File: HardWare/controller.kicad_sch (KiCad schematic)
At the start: 60 parts, among them J2 hall, J3 Conn_01x03, Q1 Q_NMOS_SGD, Q2 Q_NMOS_SGD, Q3 Q_NMOS_SGD, Q4 Q_NMOS_SGD, Q5 Q_NMOS_SGD, Q6 Q_NMOS_SGD, U2 DRV8301DCAR

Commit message: Add PCB
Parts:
- J2: footprint Connector_Molex:Molex_CLIK-Mate_502382-0570_1x05-1MP_P1.25mm_Vertical -> Connector_Molex:Molex_CLIK-Mate_502386-0570_1x05-1MP_P1.25mm_Horizontal
- J3: footprint Connector:Banana_Jack_3Pin -> USER:MR30-M
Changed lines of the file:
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@@
       (effects (font (size 1.27 1.27)) (justify left))
     )
-    (property "Footprint" "Connector_Molex:Molex_CLIK-Mate_502382-0570_1x05-1MP_P1.25mm_Vertical" (id 2) (at 269.24 36.83 0)
+    (property "Footprint" "Connector_Molex:Molex_CLIK-Mate_502386-0570_1x05-1MP_P1.25mm_Horizontal" (id 2) (at 269.24 36.83 0)
       (effects (font (size 1.27 1.27)) hide)
     )
@@
       (effects (font (size 1.27 1.27)) (justify left))
     )
-    (property "Footprint" "Connector:Banana_Jack_3Pin" (id 2) (at 274.32 121.92 0)
-      (effects (font (size 1.27 1.27)) hide)
-    )
+    (property "Footprint" "USER:MR30-M" (id 2) (at 274.32 121.92 0)
+      (effects (font (size 1.27 1.27)) hide)
+    )

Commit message: Add Rules
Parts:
- TP1: footprint TestPoint:TestPoint_THTPad_D2.0mm_Drill1.0mm -> TestPoint:TestPoint_Pad_1.0x1.0mm
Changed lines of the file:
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@@
       (effects (font (size 1.27 1.27)) (justify left))
     )
-    (property "Footprint" "TestPoint:TestPoint_THTPad_D2.0mm_Drill1.0mm" (id 2) (at 96.52 34.29 0)
+    (property "Footprint" "TestPoint:TestPoint_Pad_1.0x1.0mm" (id 2) (at 96.52 34.29 0)
       (effects (font (size 1.27 1.27)) hide)
     )

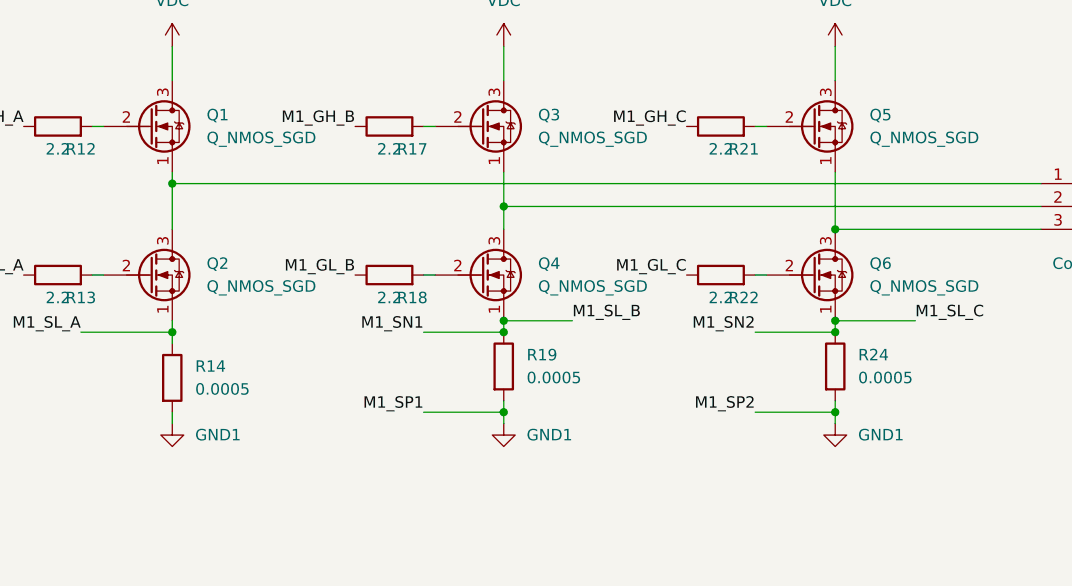
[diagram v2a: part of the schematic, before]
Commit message: 增加一些功率器件有关的pcb电路
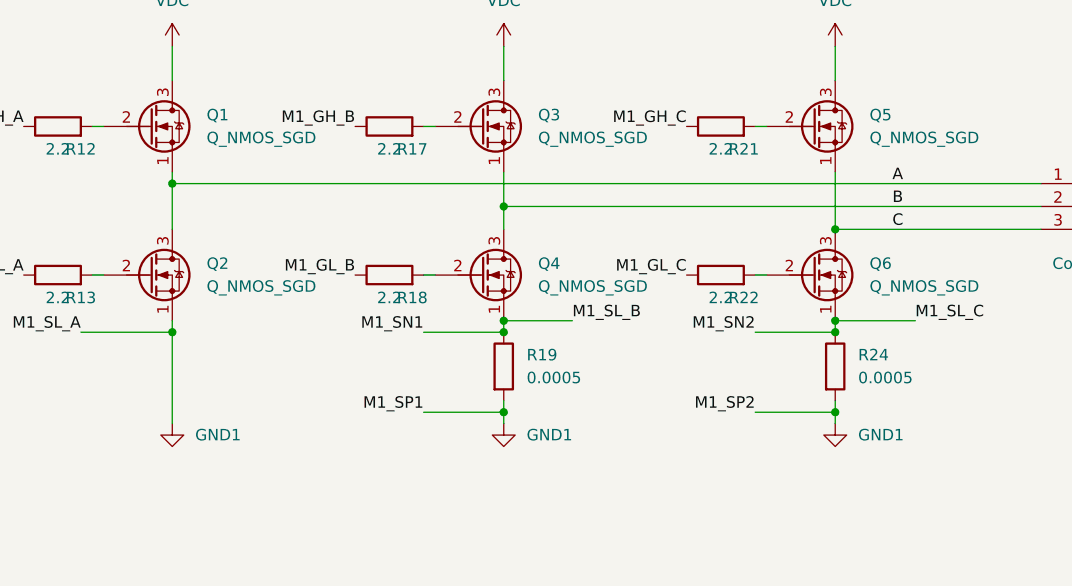
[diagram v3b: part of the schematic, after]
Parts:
- removed R14: 0.0005, Resistor_SMD:R_2512_6332Metric, symbol Device:R
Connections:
- net M1_SL_A is gone; now on net GND1: Q2.1 (S), U2.44 (SL_A)
- net A: now reaches J3.1 (Pin_1), Q1.1 (S), Q2.3 (D)
- net B: now reaches J3.2 (Pin_2), Q3.1 (S), Q4.3 (D)
- net C: now reaches J3.3 (Pin_3), Q5.1 (S), Q6.3 (D)
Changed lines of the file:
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@@
     (stroke (width 0) (type default) (color 0 0 0 0))
   )
-  (wire (pts (xy 172.72 144.78) (xy 172.72 146.05))
+  (wire (pts (xy 172.72 135.89) (xy 172.72 146.05))
     (stroke (width 0) (type default) (color 0 0 0 0))
   )
@@
     (stroke (width 0) (type default) (color 0 0 0 0))
   )
-  (wire (pts (xy 172.72 137.16) (xy 172.72 135.89))
-    (stroke (width 0) (type default) (color 0 0 0 0))
-  )
   (wire (pts (xy 240.03 36.83) (xy 264.16 36.83))
     (stroke (width 0) (type default) (color 0 0 0 0))
@@
     (effects (font (size 1.27 1.27)) (justify right bottom))
   )
+  (label "C" (at 252.73 124.46 0)
+    (effects (font (size 1.27 1.27)) (justify left bottom))
+  )
   (label "M1_GH_B" (at 193.04 113.03 180)
     (effects (font (size 1.27 1.27)) (justify right bottom))
@@
   )
   (label "SW_BST" (at 92.71 85.09 0)
+    (effects (font (size 1.27 1.27)) (justify left bottom))
+  )
+  (label "A" (at 252.73 119.38 0)
+    (effects (font (size 1.27 1.27)) (justify left bottom))
+  )
+  (label "B" (at 252.73 121.92 0)
     (effects (font (size 1.27 1.27)) (justify left bottom))
   )
@@
       (effects (font (size 1.27 1.27)) hide)
     )
-    (pin "1")
-    (pin "2")
-  )
-  (symbol (lib_id "Device:R") (at 172.72 140.97 0) (unit 1)
-    (in_bom yes) (on_board yes) (fields_autoplaced)
-    (property "Reference" "R14" (id 0) (at 175.26 139.6999 0)
-      (effects (font (size 1.27 1.27)) (justify left))
-    )
-    (property "Value" "0.0005" (id 1) (at 175.26 142.2399 0)
-      (effects (font (size 1.27 1.27)) (justify left))
-    )
-    (property "Footprint" "Resistor_SMD:R_2512_6332Metric" (id 2) (at 170.942 140.97 90)
-      (effects (font (size 1.27 1.27)) hide)
-    )
-    (property "Datasheet" "~" (id 3) (at 172.72 140.97 0)
-      (effects (font (size 1.27 1.27)) hide)
-    )

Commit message: 修改一些BUG
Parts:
- J2: footprint Connector_Molex:Molex_CLIK-Mate_502386-0570_1x05-1MP_P1.25mm_Horizontal -> USER:M1010RS-05P
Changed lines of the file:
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@@
       (effects (font (size 1.27 1.27)) (justify left))
     )
-    (property "Footprint" "Connector_Molex:Molex_CLIK-Mate_502386-0570_1x05-1MP_P1.25mm_Horizontal" (id 2) (at 269.24 36.83 0)
+    (property "Footprint" "USER:M1010RS-05P" (id 2) (at 269.24 36.83 0)
       (effects (font (size 1.27 1.27)) hide)
     )

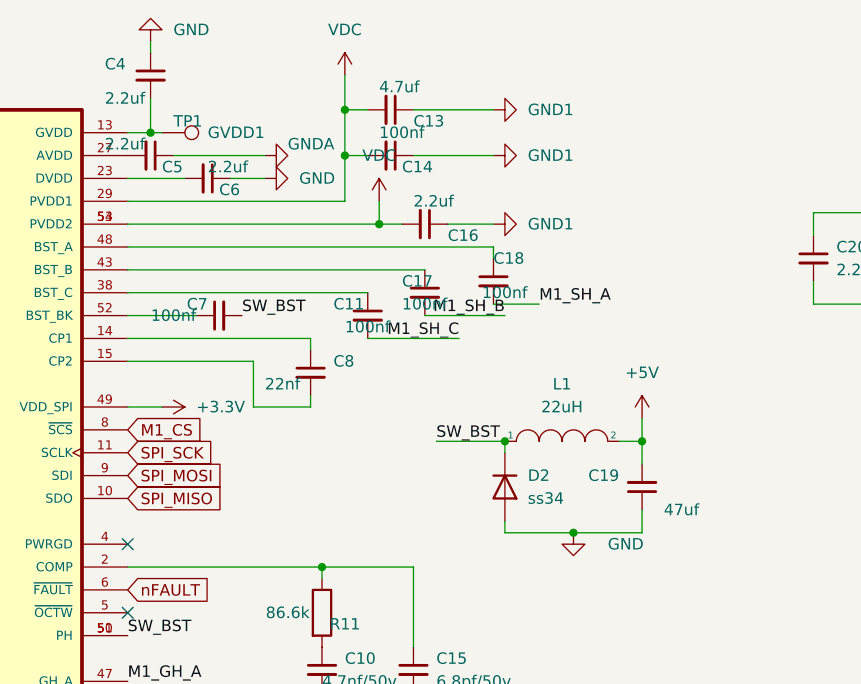
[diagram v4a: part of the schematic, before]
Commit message: 更新一些信号电源
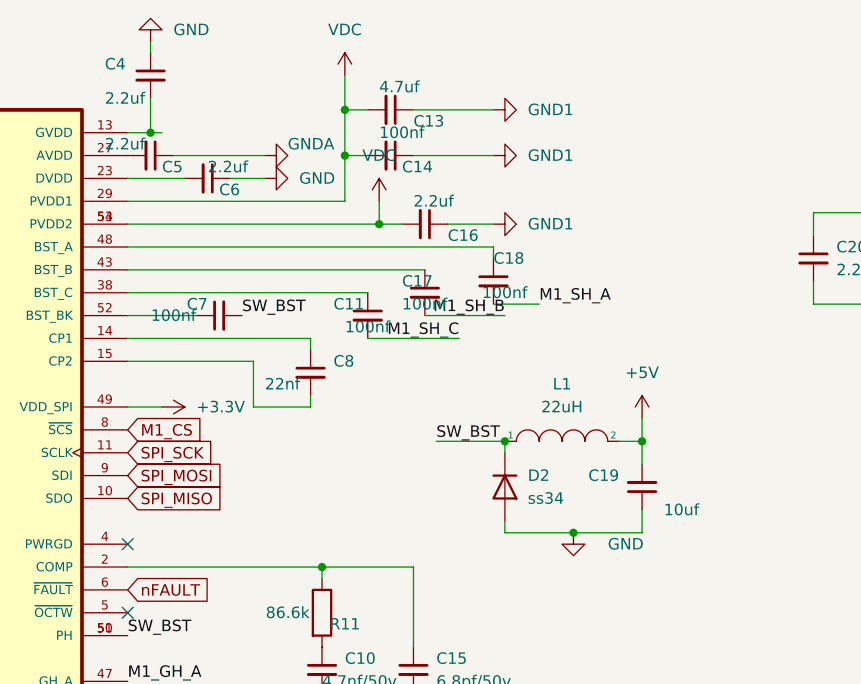
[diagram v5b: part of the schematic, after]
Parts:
- removed TP1: GVDD1, TestPoint:TestPoint_Pad_1.0x1.0mm, symbol Connector:TestPoint
- C19: value 47uf -> 10uf; footprint Capacitor_SMD:C_1812_4532Metric -> Capacitor_SMD:C_1210_3225Metric
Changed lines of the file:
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@@
       (effects (font (size 1.27 1.27)) (justify left))
     )
-    (property "Value" "47uf" (id 1) (at 156.21 71.12 0)
+    (property "Value" "10uf" (id 1) (at 156.21 71.12 0)
       (effects (font (size 1.27 1.27)) (justify left))
     )
-    (property "Footprint" "Capacitor_SMD:C_1812_4532Metric" (id 2) (at 149.86 68.58 0)
+    (property "Footprint" "Capacitor_SMD:C_1210_3225Metric" (id 2) (at 149.86 68.58 0)
       (effects (font (size 1.27 1.27)) hide)
     )
@@
     (pin "2")
   )
-  (symbol (lib_id "Connector:TestPoint") (at 96.52 29.21 270) (unit 1)
-    (in_bom yes) (on_board yes)
-    (property "Reference" "TP1" (id 0) (at 97.79 27.94 90)
-      (effects (font (size 1.27 1.27)) (justify left))
-    )
-    (property "Value" "GVDD1" (id 1) (at 101.6 29.21 90)
-      (effects (font (size 1.27 1.27)) (justify left))
-    )
-    (property "Footprint" "TestPoint:TestPoint_Pad_1.0x1.0mm" (id 2) (at 96.52 34.29 0)
-      (effects (font (size 1.27 1.27)) hide)
-    )
-    (property "Datasheet" "~" (id 3) (at 96.52 34.29 0)
-      (effects (font (size 1.27 1.27)) hide)
-    )
-    (pin "1")
-  )
   (symbol (lib_id "Device:C_Small") (at 113.03 113.03 0) (unit 1)
